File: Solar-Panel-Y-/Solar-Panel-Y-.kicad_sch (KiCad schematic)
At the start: 77 parts, among them J1 FTS-105-01-L-DV-A, J2 BM02B-SRSS-TB, Q1 BSS138DWQ-7, Q2 MBT2222ADW1T1, Q3 BSS138DWQ-7, Q4 MBT2222ADW1T1, SW1 SW_SPDT, SW2 SW_SPDT, U1 BQ25570RGRR, U2 TSL2561

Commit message: Finished Y- 4 Layer Board
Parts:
- SW1: value SW_SPDT -> D2F-L2-A1
- SW2: value SW_SPDT -> D2F-L2-A
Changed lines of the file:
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@@
   (title_block
     (title "PyCubed Mini")
-    (date "2022-06-14")
-    (rev "05")
+    (date "2022-09-01")
+    (rev "Rev B/02")
     (company "REx Lab Carnegie Mellon University")
     (comment 1 "Z.Manchester")
@@
     (stroke (width 0) (type default) (color 0 0 0 0))
   )
-  (wire (pts (xy 234.315 147.193) (xy 238.125 147.193))
+  (wire (pts (xy 232.41 147.193) (xy 236.22 147.193))
     (stroke (width 0) (type default) (color 0 0 0 0))
   )
@@
     (stroke (width 0) (type default) (color 0 0 0 0))
   )
-  (wire (pts (xy 238.125 150.749) (xy 238.125 156.083))
+  (wire (pts (xy 236.22 150.749) (xy 236.22 156.083))
     (stroke (width 0) (type default) (color 0 0 0 0))
   )
@@
     (stroke (width 0) (type default) (color 0 0 0 0))
   )
-  (wire (pts (xy 234.315 150.749) (xy 238.125 150.749))
+  (wire (pts (xy 232.41 150.749) (xy 236.22 150.749))
     (stroke (width 0) (type default) (color 0 0 0 0))
   )
@@
     (stroke (width 0) (type default) (color 0 0 0 0))
   )
-  (wire (pts (xy 238.125 147.193) (xy 238.125 142.113))
+  (wire (pts (xy 236.22 147.193) (xy 236.22 142.113))
     (stroke (width 0) (type default) (color 0 0 0 0))
   )
@@
     (stroke (width 0) (type default) (color 0 0 0 0))
   )
+  (wire (pts (xy 236.22 142.113) (xy 238.125 142.113))
+    (stroke (width 0) (type default) (color 0 0 0 0))
+  )
   (wire (pts (xy 42.418 66.04) (xy 51.308 66.04))
     (stroke (width 0) (type default) (color 0 0 0 0))
@@
     (stroke (width 0) (type default) (color 0 0 0 0))
   )
+  (wire (pts (xy 236.22 156.083) (xy 238.125 156.083))
+    (stroke (width 0) (type default) (color 0 0 0 0))
+  )
   (wire (pts (xy 237.236 32.385) (xy 237.236 51.435))
     (stroke (width 0) (type default) (color 0 0 0 0))
@@
     (effects (font (size 1.27 1.27)) (justify left bottom))
   )
-  (text "I2C Bus Protection - Light Sensor" (at 370.586 28.448 0)
+  (text "I2C Bus Protection - Light Sensor" (at 372.237 28.067 0)
     (effects (font (size 2.159 2.159)) (justify left bottom))
   )
@@
     )
   )
-  (global_label "BATT_N_SW" (shape output) (at 234.315 150.749 180) (fields_autoplaced)
+  (global_label "BATT_N_SW" (shape output) (at 232.41 150.749 180) (fields_autoplaced)
     (effects (font (size 1.27 1.27)) (justify right))
-    (property "Intersheet References" "${INTERSHEET_REFS}" (id 0) (at 221.7703 150.8284 0)
+    (property "Intersheet References" "${INTERSHEET_REFS}" (id 0) (at 219.8653 150.8284 0)
       (effects (font (size 1.27 1.27)) (justify right) hide)
     )
   )
-  (global_label "BATT_P_SW" (shape input) (at 234.315 147.193 180) (fields_autoplaced)
+  (global_label "BATT_P_SW" (shape input) (at 232.41 147.193 180) (fields_autoplaced)
     (effects (font (size 1.27 1.27)) (justify right))
-    (property "Intersheet References" "${INTERSHEET_REFS}" (id 0) (at 221.8308 147.1136 0)
+    (property "Intersheet References" "${INTERSHEET_REFS}" (id 0) (at 219.9258 147.1136 0)
       (effects (font (size 1.27 1.27)) (justify right) hide)
     )
@@
     (in_bom yes) (on_board yes)
     (property "Reference" "SW1" (id 0) (at 243.205 134.874 0))
-    (property "Value" "SW_SPDT" (id 1) (at 243.205 137.1854 0))
+    (property "Value" "D2F-L2-A1" (id 1) (at 243.205 137.1854 0))
     (property "Footprint" "solarpanels:D2F-L2-A1" (id 2) (at 243.205 142.113 0)
       (effects (font (size 1.27 1.27)) hide)
@@
     (in_bom yes) (on_board yes)
     (property "Reference" "SW2" (id 0) (at 243.205 148.844 0))
-    (property "Value" "SW_SPDT" (id 1) (at 243.205 151.1554 0))
+    (property "Value" "D2F-L2-A" (id 1) (at 243.205 151.1554 0))
     (property "Footprint" "solarpanels:D2F-L2-A" (id 2) (at 243.205 156.083 0)
       (effects (font (size 1.27 1.27)) hide)
@@
     (pin "2")
     (pin "6")
+    (pin "3")
+    (pin "4")
+    (pin "5")
   )
   (symbol (lib_id "Mechanical:MountingHole_Pad") (at 185.039 92.075 270) (unit 1)
@@
       (effects (font (size 1.27 1.27)) hide)
     )
+    (pin "1")
+    (pin "2")
+    (pin "6")
     (pin "3")
     (pin "4")
@@
     (pin "2")
     (pin "6")
+    (pin "3")
+    (pin "4")
+    (pin "5")
   )
   (symbol (lib_id "Mechanical:MountingHole_Pad") (at 185.039 104.521 270) (unit 1)
@@
     (pin "2")
     (pin "6")
+    (pin "3")
+    (pin "4")
+    (pin "5")
   )
   (symbol (lib_id "mainboard:BSS138DWQ-7") (at 425.323 81.915 0) (mirror y) (unit 2)
@@
       (effects (font (size 1.27 1.27)) hide)
     )
+    (pin "1")
+    (pin "2")
+    (pin "6")
     (pin "3")
     (pin "4")
@@
       (effects (font (size 1.27 1.27)) hide)
     )
+    (pin "1")
+    (pin "2")
+    (pin "6")
     (pin "3")
     (pin "4")
@@
     (pin "2")
     (pin "6")
+    (pin "3")
+    (pin "4")
+    (pin "5")
   )
   (symbol (lib_id "Device:R_US") (at 431.673 46.355 0) (unit 1)
@@
       (effects (font (size 1.27 1.27)) hide)
     )
+    (pin "1")
+    (pin "2")
+    (pin "6")
     (pin "3")
     (pin "4")
@@
     )
     (path "/00000000-0000-0000-0000-00005dc81e30"
-      (reference "SW1") (unit 1) (value "SW_SPDT") (footprint "solarpanels:D2F-L2-A1")
+      (reference "SW1") (unit 1) (value "D2F-L2-A1") (footprint "solarpanels:D2F-L2-A1")
     )
     (path "/00000000-0000-0000-0000-00005dcb22ff"
-      (reference "SW2") (unit 1) (value "SW_SPDT") (footprint "solarpanels:D2F-L2-A")
+      (reference "SW2") (unit 1) (value "D2F-L2-A") (footprint "solarpanels:D2F-L2-A")
     )
     (path "/00000000-0000-0000-0000-00005df6b470"

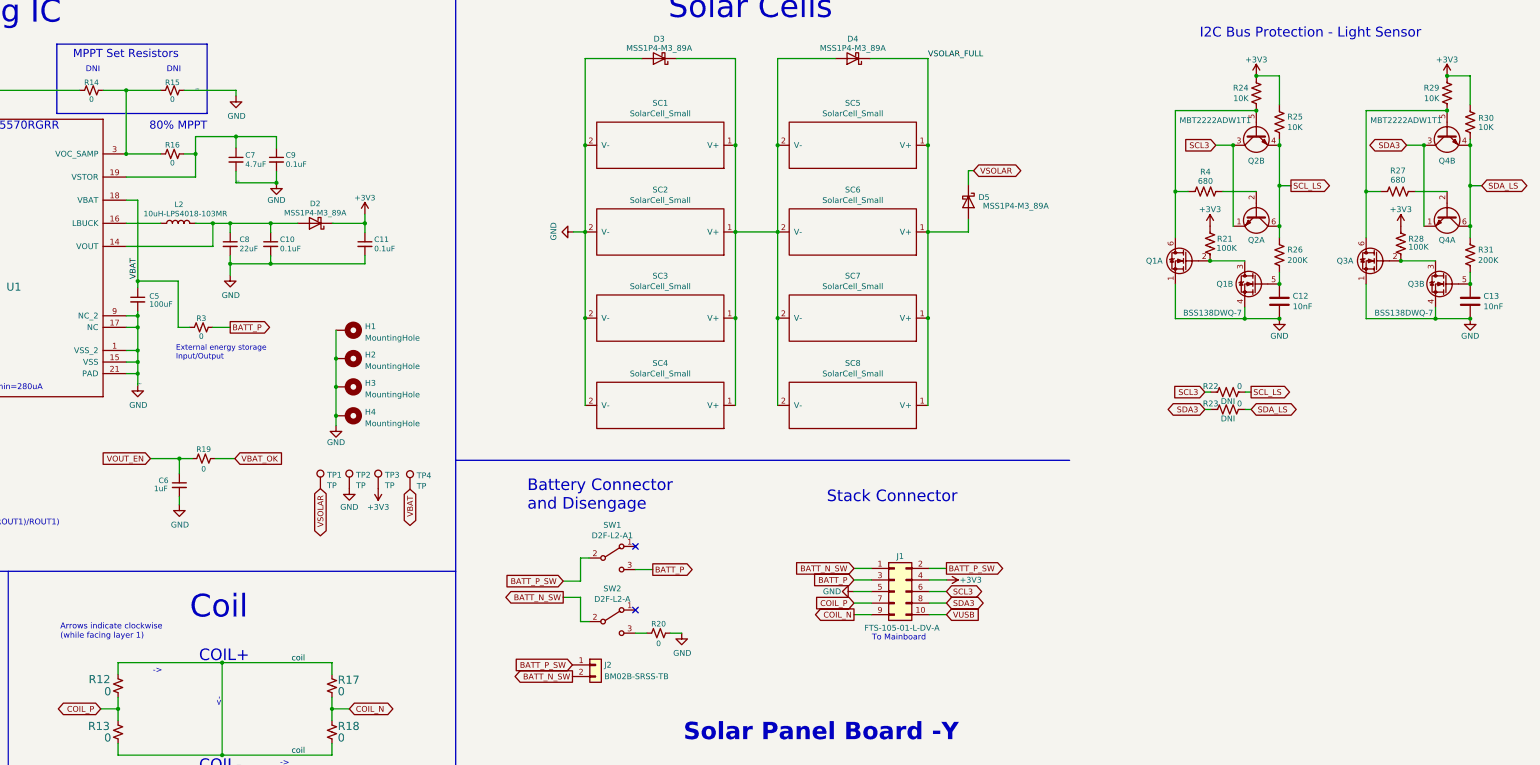
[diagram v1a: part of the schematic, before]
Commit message: Finish 6 Layer panel versions
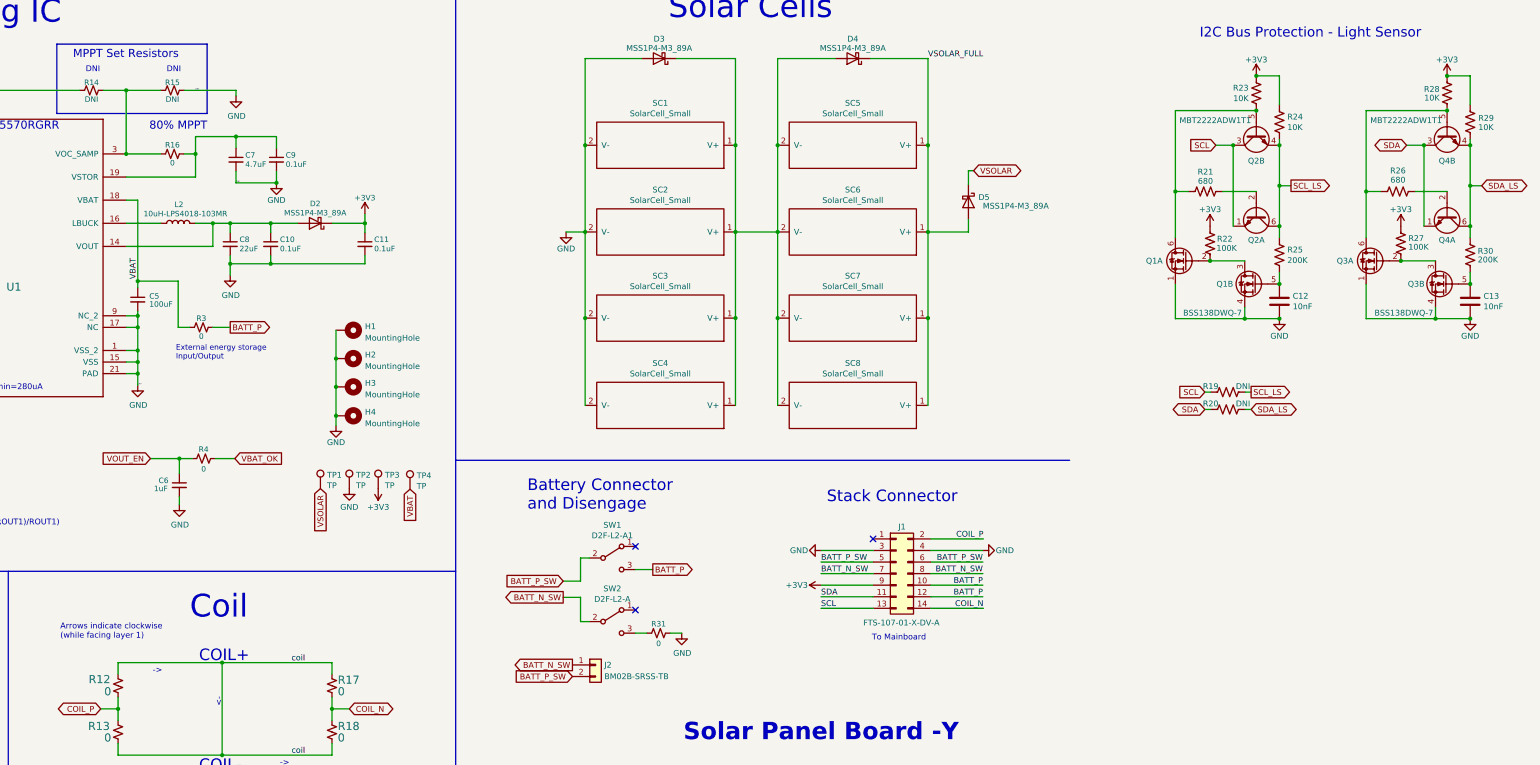
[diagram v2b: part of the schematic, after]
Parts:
- removed J1: FTS-105-01-L-DV-A, batteryboard:FTS-105-XX-YY-DV-A, symbol Connector_Generic:Conn_02x05_Odd_Even
- added J1: FTS-107-01-X-DV-A, batteryboard:SAMTEC-FTS-107-01-X-DV-A, symbol Connector_Generic:Conn_02x07_Odd_Even
- C10, C11, C12, C13, C2, C3, C4, C6, C7, C8, C9: footprint Capacitor_SMD:C_0402_1005Metric -> Capacitor_SMD:C_0603_1608Metric
- R10, R11, R12, R13, R16, R17, R18, R3, R5, R6, R7, R8, R9: footprint Resistor_SMD:R_0402_1005Metric -> Resistor_SMD:R_0603_1608Metric
- R14, R15: value 0 -> DNI; footprint Resistor_SMD:R_0402_1005Metric -> Resistor_SMD:R_0603_1608Metric
- R19: renamed from R22; value 0 -> DNI; footprint Resistor_SMD:R_0402_1005Metric -> Resistor_SMD:R_0603_1608Metric
- R20: renamed from R23; value 0 -> DNI; footprint Resistor_SMD:R_0402_1005Metric -> Resistor_SMD:R_0603_1608Metric
- R21: renamed from R4; footprint Resistor_SMD:R_0402_1005Metric -> Resistor_SMD:R_0603_1608Metric
- R22: renamed from R21; footprint Resistor_SMD:R_0402_1005Metric -> Resistor_SMD:R_0603_1608Metric
- R23: renamed from R24; footprint Resistor_SMD:R_0402_1005Metric -> Resistor_SMD:R_0603_1608Metric
- R24: renamed from R25; footprint Resistor_SMD:R_0402_1005Metric -> Resistor_SMD:R_0603_1608Metric
- R25: renamed from R26; footprint Resistor_SMD:R_0402_1005Metric -> Resistor_SMD:R_0603_1608Metric
- R26: renamed from R27; footprint Resistor_SMD:R_0402_1005Metric -> Resistor_SMD:R_0603_1608Metric
- R27: renamed from R28; footprint Resistor_SMD:R_0402_1005Metric -> Resistor_SMD:R_0603_1608Metric
- R28: renamed from R29; footprint Resistor_SMD:R_0402_1005Metric -> Resistor_SMD:R_0603_1608Metric
- R29: renamed from R30; footprint Resistor_SMD:R_0402_1005Metric -> Resistor_SMD:R_0603_1608Metric
- R30: renamed from R31; footprint Resistor_SMD:R_0402_1005Metric -> Resistor_SMD:R_0603_1608Metric
- R31: renamed from R20; footprint Resistor_SMD:R_0402_1005Metric -> Resistor_SMD:R_0603_1608Metric
- R4: renamed from R19; footprint Resistor_SMD:R_0402_1005Metric -> Resistor_SMD:R_0603_1608Metric
- renumbered SC3 to SC2, SC2 to SC3
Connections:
- net +3V3: now also J1.9 (Pin_9)
- net BATT_N_SW: now also J2.1 (Pin_1), J1.7 (Pin_7), J1.8 (Pin_8); no longer J2.2 (Pin_2)
- net BATT_P: now also J1.10 (Pin_10), J1.12 (Pin_12)
- net BATT_P_SW: now also J2.2 (Pin_2), J1.5 (Pin_5), J1.6 (Pin_6); no longer J2.1 (Pin_1)
- net COIL_N: now also J1.14 (Pin_14)
- net COIL_P: now also J1.2 (Pin_2)
- net GND: now also J1.3 (Pin_3), J1.4 (Pin_4)
- net SCL3 renamed SCL
- net SCL: now also J1.13 (Pin_13)
- net SDA3 renamed SDA
- net SDA: now also J1.11 (Pin_11)
- no-connect marks 3 -> 4
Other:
- moved on the sheet: SC2, SC3
